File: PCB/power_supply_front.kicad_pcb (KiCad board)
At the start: 2 copper layers, 200.9 x 59.7 mm, 50 parts, among them IC1 LM66200, IC2 ESDALC6V1W5, J1 Screw_Terminal_01x04, J2 VBUS/GND for the stacked PCB, J3 1935789, J4 VBUS/GND for the stacked PCB, J5 Power Supply, J6 Screw_Terminal_01x04, U10 H11L1, U6 TS3USB30EDGSR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

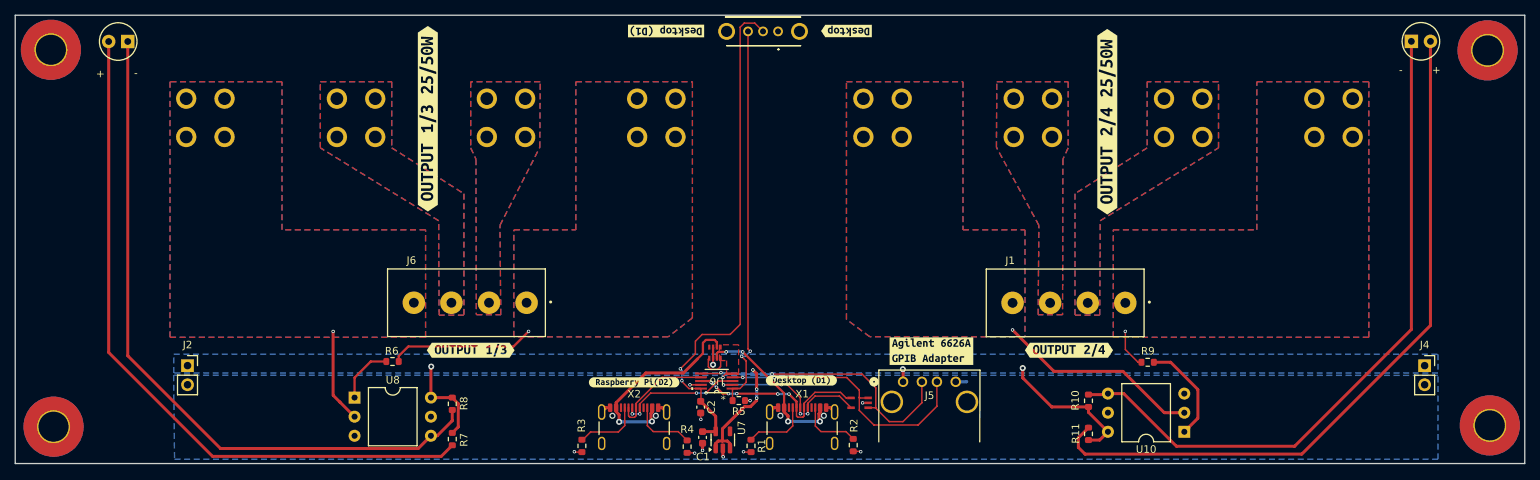
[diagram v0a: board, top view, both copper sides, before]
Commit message: Adjust plug spacing. Add label connector pinout on silkscreen.
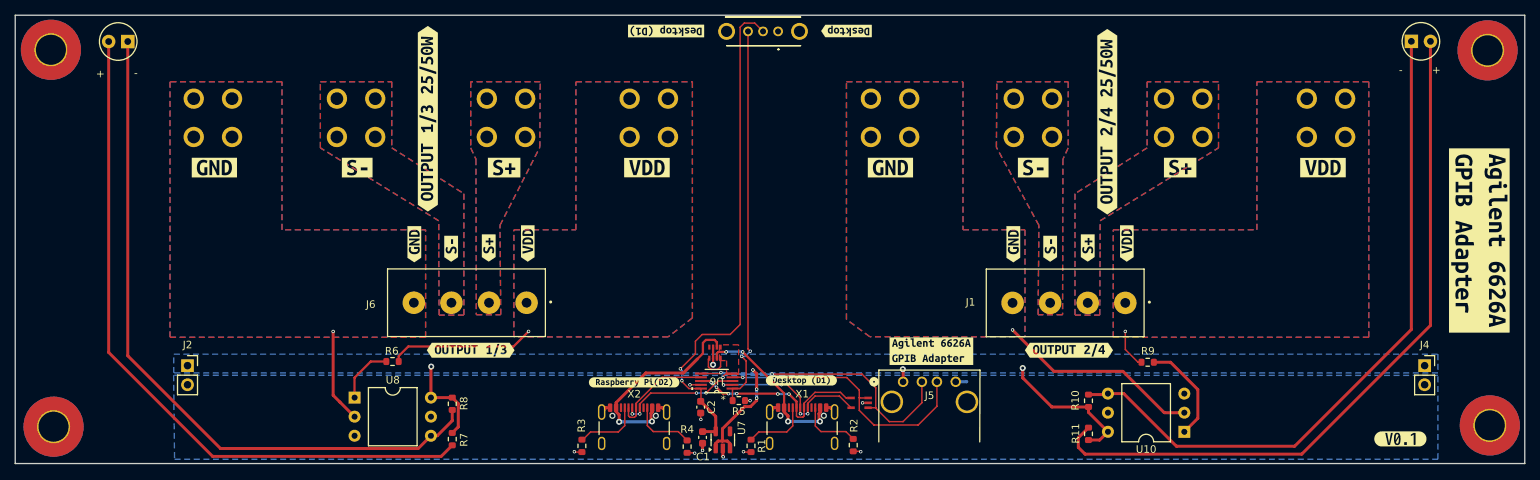
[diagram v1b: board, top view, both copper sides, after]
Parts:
- added kibuzzard-675368B8: G***, kibuzzard-675368B8, F.Cu at (173.6, 54.3)
- added kibuzzard-675368B8: G***, kibuzzard-675368B8, F.Cu at (93.9, 54.3)
- added kibuzzard-675368D0: G***, kibuzzard-675368D0, F.Cu at (78.8, 54.4)
- added kibuzzard-675368D0: G***, kibuzzard-675368D0, F.Cu at (158.5, 54.4)
- added kibuzzard-675368D9: G***, kibuzzard-675368D9, F.Cu at (163.4, 55.0)
- added kibuzzard-675368D9: G***, kibuzzard-675368D9, F.Cu at (83.7, 55.0)
- added kibuzzard-675368DE: G***, kibuzzard-675368DE, F.Cu at (168.4, 54.9)
- added kibuzzard-675368DE: G***, kibuzzard-675368DE, F.Cu at (88.7, 54.9)
- added kibuzzard-675369A2: G***, kibuzzard-675369A2, F.Cu at (52.2, 44.2)
- added kibuzzard-675369A2: G***, kibuzzard-675369A2, F.Cu at (142.2, 44.2)
- added kibuzzard-675369E9: G***, kibuzzard-675369E9, F.Cu at (161.2, 44.2)
- added kibuzzard-675369E9: G***, kibuzzard-675369E9, F.Cu at (71.2, 44.2)
- added kibuzzard-675369FB: G***, kibuzzard-675369FB, F.Cu at (90.8, 44.2)
- added kibuzzard-675369FB: G***, kibuzzard-675369FB, F.Cu at (180.7, 44.2)
- added kibuzzard-67536A0A: G***, kibuzzard-67536A0A, F.Cu at (199.7, 44.2)
- added kibuzzard-67536A0A: G***, kibuzzard-67536A0A, F.Cu at (109.8, 44.2)
- added kibuzzard-67536AC1: G***, kibuzzard-67536AC1, F.Cu at (210.0, 80.3)
- added kibuzzard-67536BD6: G***, kibuzzard-67536BD6, F.Cu at (220.5, 53.9)
- moved U1 1.00 mm to (72.8, 26.8)
- moved U12 1.00 mm to (200.9, 26.8)
- moved U2 1.00 mm to (110.8, 26.8)
- moved U3 1.00 mm to (142.9, 26.8)
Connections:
- J1 pad 2: S2- -> S2+
- J1 pad 3: S2+ -> S2-
- J6 pad 2: S1- -> S1+
- J6 pad 3: S1+ -> S1-
- U11 pad 1: S1- -> S1+
- U11 pad 2: S1- -> S1+
- U11 pad 3: S1- -> S1+
- U11 pad 4: S1- -> S1+
- U4 pad 1: S2+ -> S2-
- U4 pad 2: S2+ -> S2-
- U4 pad 3: S2+ -> S2-
- U4 pad 4: S2+ -> S2-
- U5 pad 1: S2- -> S2+
- U5 pad 2: S2- -> S2+
- U5 pad 3: S2- -> S2+
- U5 pad 4: S2- -> S2+
- U9 pad 1: S1+ -> S1-
- U9 pad 2: S1+ -> S1-
- U9 pad 3: S1+ -> S1-
- U9 pad 4: S1+ -> S1-

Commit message: PCB: Small adjustments.
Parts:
- added kibuzzard-6759F0B5: G***, kibuzzard-6759F0B5, B.Cu at (221.9, 53.7)
